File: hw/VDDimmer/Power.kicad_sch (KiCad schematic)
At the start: 33 parts, among them J2 VIN 12V, Q5 SUD50P06-15, U2 AP63301WU-7, U3 BL1117-33CX

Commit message: Mark R30 DNP and move L1/L3 to a curated inductor land (schematic side)
R30 -> DNP
----------
R30 is the input LC filter's bypass jumper, in parallel with L3. The filter is
populated per the 2026-08-29 decision, so fitting R30 shorts L3 out. Recorded
in its Assembly field and in bom-lcsc.csv; export-cpl.sh now excludes it, and
the CPL drops 78 -> 77 machine-placed parts. The real (dnp yes) attribute still
needs setting in the GUI -- cpl.py reports R30 as excluded "on a text marker
only" to keep that visible.

This also closes the old "confirm a 0R jumper rated >= 2 A" question: an
unfitted part carries no current. C17477 is 125 mW with no published current
rating -- fine as a DNP, unusable as a 1.2 A jumper.

L1/L3 land
----------
The previous footprint, VANDIMMER:L_cjiang_FXL0630_7.0x6.6mm, was
Konnect-generated and internally inconsistent: named for an FXL0630 (a 6.0 mm
body) but described as 7.0 x 6.6 mm. Its pads were 2.50 x 6.00 on a 4.90 mm
pitch.

KiCad's curated library disagrees, and three independent 6x6 lands agree with
each other exactly:

  L_Changjiang_FXL0630        2.35 x 3.50  pitch 6.05
  L_Chilisin_BMRx00060630     2.35 x 3.50  pitch 6.05
  L_Chilisin_BMRB00060650     2.35 x 3.50  pitch 6.05

So the custom land sat 1.15 mm too close together. A real 6x6 inductor's
terminals span 1.85-4.20 mm from the centreline while those pads spanned
1.20-3.70 mm, leaving ~0.5 mm of each terminal over bare board.

L1 and L3 now use Inductor_SMD:L_Changjiang_FXL0630. Verified offline before
committing: with the new land at the existing centres, all four pads are clear
of every foreign net; the only copper within 0.5 mm belongs to their own nets
(SW, +5V, VIN_PROT, VIN_BUCK) and to +5V pads C25.1/C26.1.

The part stays PNLS6045-100M. It is the best of only three 10uH parts JLC
stocks in 6x6 at >= 3.5 A: 4.5 A Isat, 57 mOhm, $0.07, 5539 in stock. The
alternative considered, MSA75-100M, was abandoned because its recommended-layout
dimensions are vector art in the da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
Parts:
- L1: footprint VANDIMMER:L_cjiang_FXL0630_7.0x6.6mm -> Inductor_SMD:L_Changjiang_FXL0630; Assembly CANDIDATE ONLY - verify land pattern. Board land is two 2.5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 -> Land is KiCad's curated Inductor_SMD:L_Changjiang_FXL0630 (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
- L3: footprint VANDIMMER:L_cjiang_FXL0630_7.0x6.6mm -> Inductor_SMD:L_Changjiang_FXL0630; Assembly NOW FITTED per the 2026-08-29 decision, no longer DNP. Same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 -> Land is KiCad's curated Inductor_SMD:L_Changjiang_FXL0630 (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
- R30: Assembly 0 R jumper carrying ~1.2 A - confirm the part's current rat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 -> DNP - bypass jumper in parallel with L3. The input LC filte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
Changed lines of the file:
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@@
 			)
 		)
-		(property "Footprint" "VANDIMMER:L_cjiang_FXL0630_7.0x6.6mm"
+		(property "Footprint" "Inductor_SMD:L_Changjiang_FXL0630"
 			(at 41.91 95.25 0)
 			(hide yes)
@@
 			)
 		)
-		(property "Assembly" "NOW FITTED per the 2026-08-29 decision, no longer DNP. Same land-pattern caveat as L1"
+		(property "Assembly" "Land is KiCad's curated Inductor_SMD:L_Changjiang_FXL0630 (2.35 x 3.50 pads, 6.05 pitch). Input LC filter inductor - fitted per the 2026-08-29 decision, with R30 (its bypass jumper) DNP"
 			(at 41.91 95.25 0)
 			(hide yes)
@@
 			)
 		)
-		(property "Assembly" "0 R jumper carrying ~1.2 A - confirm the part's current rating against its datasheet; JLC lists only 125 mW"
+		(property "Assembly" "DNP - bypass jumper in parallel with L3. The input LC filter is populated per the 2026-08-29 decision, so fitting R30 shorts L3 out and there is no filter. Needs KiCad's (dnp yes) attribute set in the GUI; no MCP tool writes it"
 			(at 41.91 111.76 0)
 			(hide yes)
@@
 			)
 		)
-		(property "Footprint" "VANDIMMER:L_cjiang_FXL0630_7.0x6.6mm"
+		(property "Footprint" "Inductor_SMD:L_Changjiang_FXL0630"
 			(at 237.49 76.2 0)
 			(hide yes)
@@
 			)
 		)
-		(property "Assembly" "CANDIDATE ONLY - verify land pattern. Board land is two 2.50 x 6.00 mm pads on 4.90 mm centres; this part is a 6x6 mm body. DCR 57 mOhm costs 0.51 W at 3 A"
+		(property "Assembly" "Land is KiCad's curated Inductor_SMD:L_Changjiang_FXL0630 (2.35 x 3.50 pads, 6.05 pitch), NOT the earlier Konnect-generated VANDIMMER footprint whose pads sat 1.15 mm too close together. Fitted part is PNLS6045-100M, 6.0 x 6.0 x 4.5 mm"
 			(at 237.49 76.2 0)
 			(hide yes)

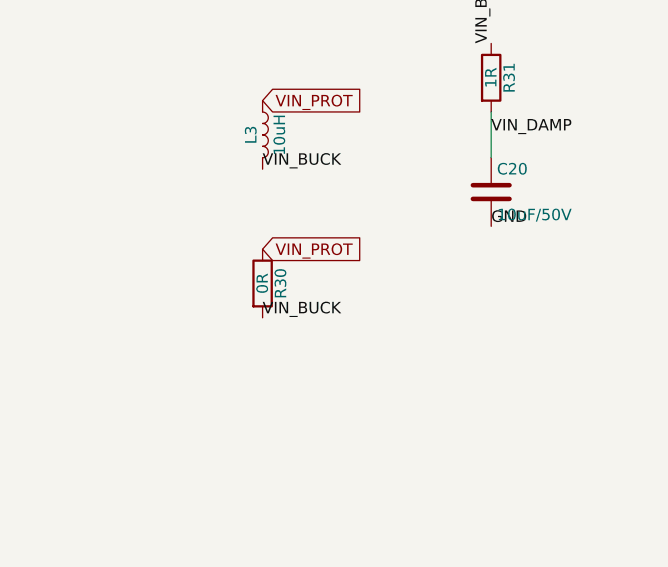
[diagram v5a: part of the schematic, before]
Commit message: Swap L1/L3 to a curated inductor land, repair routing, clear the courtyard errors
Board side of the change committed at 9b703c8. L1 and L3 now carry
Inductor_SMD:L_Changjiang_FXL0630 (2.35 x 3.50 pads, 6.05 pitch) in place of the
Konnect-generated VANDIMMER footprint whose pads sat 1.15 mm too close together.
R30's (dnp yes) is set, so all three DNPs now report via KiCad's own attribute
rather than a text marker.

Routing repairs
---------------
The old pads were 6.00 mm tall; the new ones are 3.50 mm. Two connections were
caught only by that extra height and broke on the swap:

  L1.2 (+5V)      the two 1.5 mm horizontals end at y=71.5 and y=76.5, outside
                  the new pad's 72.25-75.75 band
  VIN_BUCK        the x=161.0 spine's top end at y=69.5 was bridged by the old
                  L3.2 pad, which reached y=69.5; the new one stops at 68.25

Fixed with two short 1.5 mm tracks, both validated by route.py before pushing.
connect.py then returned to the baseline 12 split nets, with L1.2 back in +5V
group 0 and L3.1 in VIN_PROT group 0 (both via zone fill, which is why a
track-contact check alone still showed them as bare).

Courtyard errors
----------------
The wider land (8.90 mm courtyard vs 7.90) pushed L1's courtyard wings 0.25 mm
into C25 and C26 -- two DRC errors, the first this board has had. Pad clearance
had been checked against every foreign net and was clean; courtyards had not
been. That is the gap.

C25/C26 moved 0.4 mm east rather than moving L1: nothing but board edge lies
east of them, whereas C24's bootstrap cap is 1.25 mm west of L1 and L1 sits in
the switching path. All four moved pads keep their existing track contacts and
conflict with no foreign net. Courtyard gap is now 0.150 mm.

tools/fpspace.py gains --courtyards, a whole-board overlap sweep, negative-tested
against the pre-fix geometry where it reports both overlaps.

Verification
------------
  DRC          0 errors, 166 warnings, 15 unconnected, schematic parity 0
  connect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
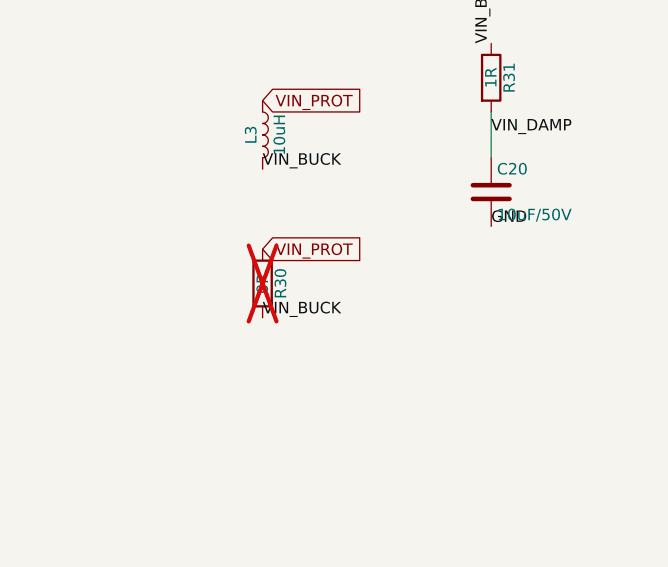
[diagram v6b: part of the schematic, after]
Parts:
- R30: now not fitted
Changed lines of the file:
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@@
 		(on_board yes)
 		(in_pos_files yes)
-		(dnp no)
+		(dnp yes)
 		(property "Reference" "R30"
 			(at 43.942 111.76 90)

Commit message: Revert the L1/L3 land change: the original geometry was correct
Commits 9b703c8 and 4760f5e moved L1/L3 to KiCad's curated
Inductor_SMD:L_Changjiang_FXL0630 on the reasoning that three independent
curated 6x6 lands agreed with each other and disagreed with the project's
custom footprint. That reasoning was wrong, and installing poppler made it
possible to prove so from the fitted part's own datasheet.

DMBJ PNLS6045, datasheet p3 dimension table: body A=6.0, B=6.0, C(max)=4.50,
terminals D=5.0 x E=1.65 mm. So each terminal spans 1.35-3.00 mm from the
centreline and is 5.0 mm wide.

  land                                pad span    contact       area   of terminal
  L_cjiang_FXL0630_7.0x6.6mm (ours)  1.20-3.70   1.65 x 5.00   8.25    100 %
  Inductor_SMD:L_Changjiang_FXL0630  1.85-4.20   1.15 x 3.50   4.03     49 %

The custom land covers the whole terminal with a 0.70 mm toe. KiCad's covers
half of it and puts 1.20 mm of pad past the body edge. KiCad's land is correct
for an FXL0630 -- a different part -- and must not be used for a PNLS6045.

What went wrong: the footprint is MISNAMED. It is a 6045 land called
L_cjiang_FXL0630_7.0x6.6mm, and it was judged by that name and by comparison
with curated lands for the part the name refers to, without ever checking the
terminal dimensions of the part actually fitted. A curated library land is only
authority for the part it is named after.

The footprint's descr now opens with "MISNAMED - this is a 6045 land, NOT an
FXL0630 7.0x6.6", records the verified terminal geometry, and warns against
substituting KiCad's version. Pads confirmed untouched by that edit. The
filename was left alone deliberately: renaming would mean another schematic
field change, another F8 sync and another round of re-verification, for no
change to the board.

Not reverted, deliberately: C25/C26 stay at x=192.9 (moved 0.4 mm east while the
wider land was fitted). Harmless now the narrower courtyard is back, already
verified there, and moving them again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
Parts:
- L1, L3: footprint Inductor_SMD:L_Changjiang_FXL0630 -> VANDIMMER:L_cjiang_FXL0630_7.0x6.6mm; Assembly Land is KiCad's curated Inductor_SMD:L_Changjiang_FXL0630 (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 -> Land VERIFIED against the PNLS6045 datasheet (p3): terminal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
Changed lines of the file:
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@@
 			)
 		)
-		(property "Footprint" "Inductor_SMD:L_Changjiang_FXL0630"
+		(property "Footprint" "VANDIMMER:L_cjiang_FXL0630_7.0x6.6mm"
 			(at 41.91 95.25 0)
 			(hide yes)
@@
 			)
 		)
-		(property "Assembly" "Land is KiCad's curated Inductor_SMD:L_Changjiang_FXL0630 (2.35 x 3.50 pads, 6.05 pitch). Input LC filter inductor - fitted per the 2026-08-29 decision, with R30 (its bypass jumper) DNP"
+		(property "Assembly" "Land VERIFIED against the PNLS6045 datasheet (p3): terminals D=5.0 x E=1.65 mm, covered 100% by these pads. Input LC filter inductor, fitted per the 2026-08-29 decision with R30 (its bypass jumper) DNP. NOTE the footprint NAME is wrong - it is a 6045 land, not an FXL0630 7.0x6.6"
 			(at 41.91 95.25 0)
 			(hide yes)
@@
 			)
 		)
-		(property "Footprint" "Inductor_SMD:L_Changjiang_FXL0630"
+		(property "Footprint" "VANDIMMER:L_cjiang_FXL0630_7.0x6.6mm"
 			(at 237.49 76.2 0)
 			(hide yes)
@@
 			)
 		)
-		(property "Assembly" "Land is KiCad's curated Inductor_SMD:L_Changjiang_FXL0630 (2.35 x 3.50 pads, 6.05 pitch), NOT the earlier Konnect-generated VANDIMMER footprint whose pads sat 1.15 mm too close together. Fitted part is PNLS6045-100M, 6.0 x 6.0 x 4.5 mm"
+		(property "Assembly" "Land VERIFIED against the PNLS6045 datasheet (p3): terminals are D=5.0 x E=1.65 mm on a 6.0 x 6.0 body, spanning 1.35-3.00 mm from centreline. These pads (2.50 x 6.00 at +/-2.45, spanning 1.20-3.70) cover 100% of the terminal with a 0.70 mm toe. NOTE the footprint NAME is wrong - it is a 6045 land, not an FXL0630 7.0x6.6"
 			(at 237.49 76.2 0)
 			(hide yes)

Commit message: Swap the five 10uF 1210s from 100 V to 50 V: -$1.44/board
The board carried FS32X106K101EGG (C5156756), a 100 V 1210, at $0.4774 -- five
per board, 20% of the whole BOM, on a board that is 12 V only. Replaced with
HGC1210R7106M500NSVK (C33546018), 10uF 50V X7R +/-20%, $0.1901, stock 16809.

  component cost   $11.886 -> $10.450 per board   (saving $1.44)

Voltage margin checked rather than assumed. All five sit on 12 V-class rails:

  C20        VIN_DAMP            input LC filter
  C21, C22   VIN_BUCK            buck input capacitors
  C63, C64   ADDR1/2_VOUT        switchable 12 V or 5 V via J9/J10

and D5, the SMBJ18A, clamps input transients at 29.2 V -- comfortably under the
50 V rating. The 1210 land is unchanged; both parts share the same EasyEDA
footprint UUID.

Deliberately NOT the 25 V part (C39232, $0.1303, a further $0.30/board): C21/C22
are the buck's input capacitors and a 25 V X7R 1210 loses 40-60% of its
capacitance at 12 V DC bias. At 50 V with +/-20% tolerance the pair still gives
roughly 13-14 uF effective, against the AP63301's ~10 uF want.

Incidental tidy-up: the schematic Values already read "10uF/50V", so the 100 V
part was the one out of step. They now agree.

Leaves schematic parity at 5 -- the LCSC field differs between schematic and
board footprint for these five caps. Cosmetic; BOM and CPL are generated from
the schematic, so the fab data is correct. One F8 sync clears it.

ERC 0, DRC 0 errors, 165 warnings, 15 unconnected. JLC bundle regenerated.

Co-Authored-By: Claude Opus 5 (1M context) <noreply@anthropic.com>
Claude-Session: https://claude.ai/code/session_01AnYUdWpnpbT2cnPRPqtfVa
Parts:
- C20, C21, C22: LCSC C5156756 -> C33546018; MPN FS32X106K101EGG -> HGC1210R7106M500NSVK; Manufacturer PSA -> Chinocera
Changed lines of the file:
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@@
 			)
 		)
-		(property "LCSC" "C5156756"
+		(property "LCSC" "C33546018"
 			(at 165.1 105.41 0)
 			(hide yes)
@@
 			)
 		)
-		(property "MPN" "FS32X106K101EGG"
+		(property "MPN" "HGC1210R7106M500NSVK"
 			(at 165.1 105.41 0)
 			(hide yes)
@@
 			)
 		)
-		(property "Manufacturer" "PSA"
+		(property "Manufacturer" "Chinocera"
 			(at 165.1 105.41 0)
 			(hide yes)
@@
 			)
 		)
-		(property "LCSC" "C5156756"
+		(property "LCSC" "C33546018"
 			(at 67.31 101.6 0)
 			(hide yes)
@@
 			)
 		)
-		(property "MPN" "FS32X106K101EGG"
+		(property "MPN" "HGC1210R7106M500NSVK"
 			(at 67.31 101.6 0)
 			(hide yes)
@@
 			)
 		)
-		(property "Manufacturer" "PSA"
+		(property "Manufacturer" "Chinocera"
 			(at 67.31 101.6 0)
 			(hide yes)
@@
 			)
 		)
-		(property "LCSC" "C5156756"
+		(property "LCSC" "C33546018"
 			(at 149.86 105.41 0)
 			(hide yes)
@@
 			)
 		)
-		(property "MPN" "FS32X106K101EGG"
+		(property "MPN" "HGC1210R7106M500NSVK"
 			(at 149.86 105.41 0)
 			(hide yes)
@@
 			)
 		)
-		(property "Manufacturer" "PSA"
+		(property "Manufacturer" "Chinocera"
 			(at 149.86 105.41 0)
 			(hide yes)
